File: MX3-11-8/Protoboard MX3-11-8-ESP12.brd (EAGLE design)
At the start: 74.4 x 99.4 mm, 638 parts, among them J1 DCJ0202, X3 RJ45

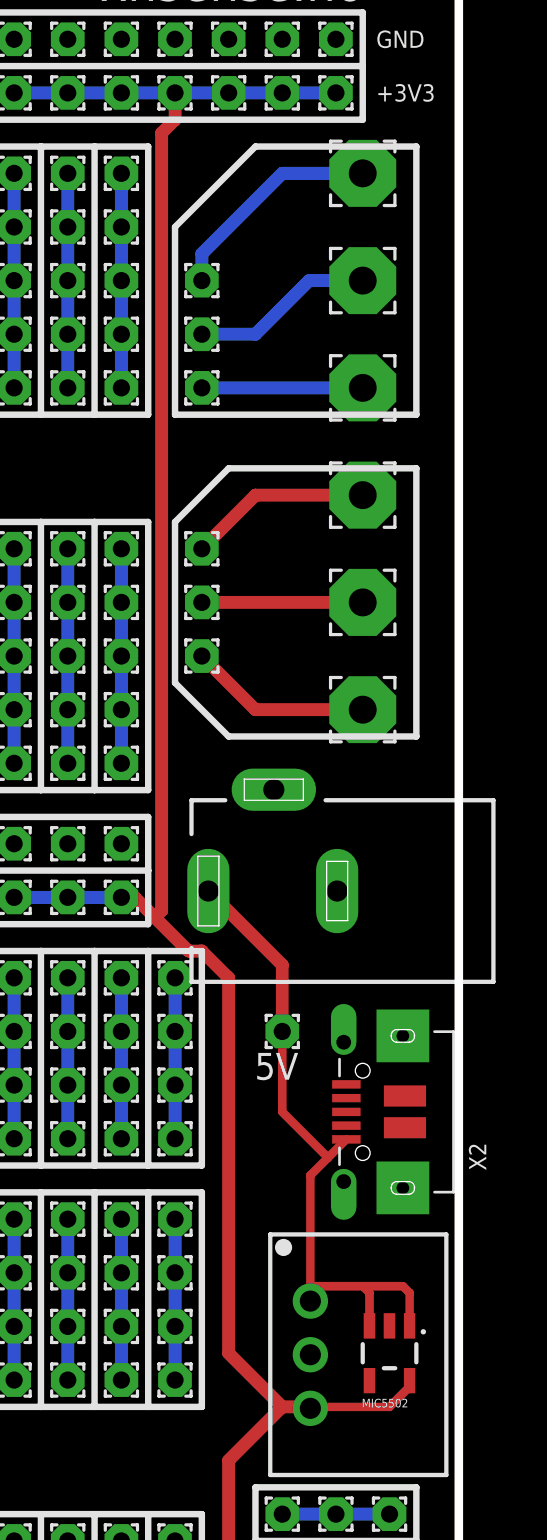
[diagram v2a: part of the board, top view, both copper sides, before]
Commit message: Change usb connector
Change to correct usb connecter and moved esp8266 bit more onto the
board.
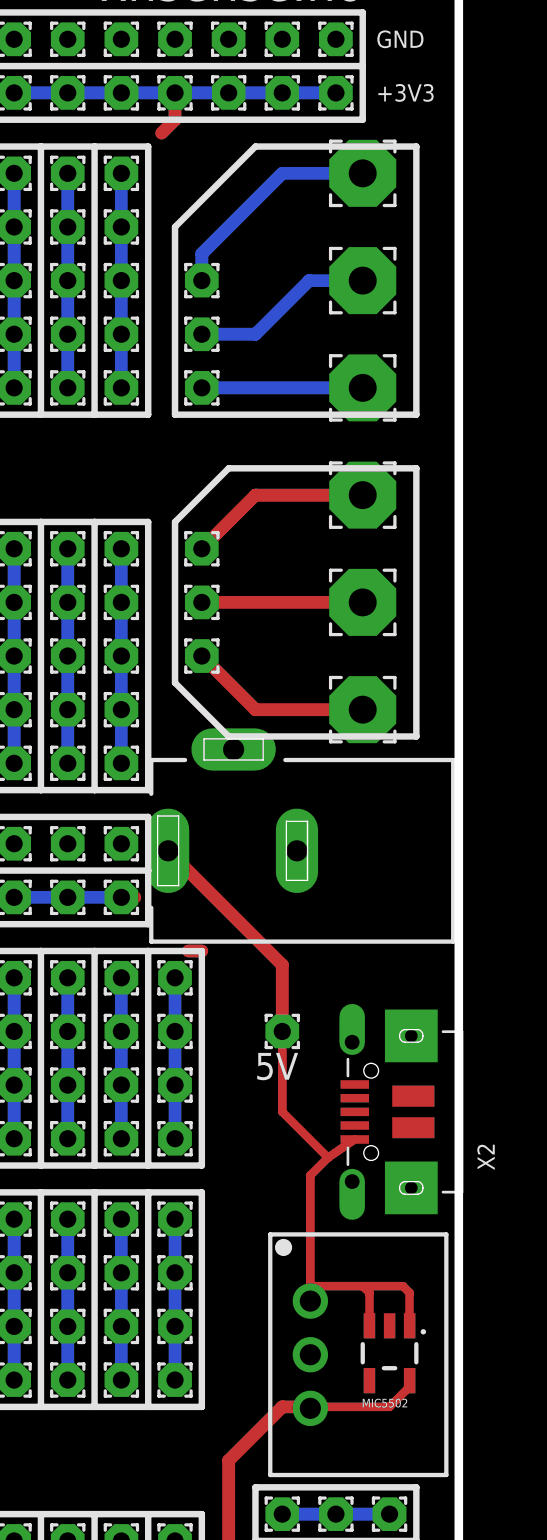
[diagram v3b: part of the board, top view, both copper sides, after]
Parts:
- moved J1 2.69 mm to (63.7, 56.8)
- moved X2 0.40 mm to (70.2, 44.5)
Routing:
- net VDD: track 304.0 -> 239.9 mm
- net VCC: track 31.7 -> 34.7 mm
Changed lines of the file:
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@@
 <attribute name="VALUE" x="17.78" y="6.95" size="0.0254" layer="27"/>
 </element>
-<element name="J1" library="con-jack" package="DCJ0202" value="DCJ0202" x="65.64" y="54.91" smashed="yes" rot="R90">
-<attribute name="MPN" value="" x="65.64" y="54.91" size="1.778" layer="27" rot="R90" display="off"/>
-<attribute name="OC_NEWARK" value="unknown" x="65.64" y="54.91" size="1.778" layer="27" rot="R90" display="off"/>
-<attribute name="MF" value="" x="65.64" y="54.91" size="1.778" layer="27" rot="R90" display="off"/>
-<attribute name="OC_FARNELL" value="unknown" x="65.64" y="54.91" size="1.778" layer="27" rot="R90" display="off"/>
+<element name="J1" library="con-jack" package="DCJ0202" value="DCJ0202" x="63.735" y="56.815" smashed="yes" rot="R90">
+<attribute name="MPN" value="" x="63.735" y="56.815" size="1.778" layer="27" rot="R90" display="off"/>
+<attribute name="OC_NEWARK" value="unknown" x="63.735" y="56.815" size="1.778" layer="27" rot="R90" display="off"/>
+<attribute name="MF" value="" x="63.735" y="56.815" size="1.778" layer="27" rot="R90" display="off"/>
+<attribute name="OC_FARNELL" value="unknown" x="63.735" y="56.815" size="1.778" layer="27" rot="R90" display="off"/>
 </element>
 <element name="DC" library="dc-dc-converter" package="SIP3" value="R-78C1.8-1.0" x="67.37" y="32.95" smashed="yes" rot="R270"/>
@@
 <attribute name="VALUE" x="25.4" y="79.34" size="0.0254" layer="27"/>
 </element>
-<element name="X2" library="microbuilder" package="4UCONN_20329" value="" x="69.85" y="44.45" rot="R90"/>
+<element name="X2" library="microbuilder" package="4UCONN_20329" value="" x="70.25" y="44.45" rot="R90"/>
 <element name="MIC5502" library="SparkFun-PowerIC" package="SOT23-5" value="" x="71.12" y="33.02" rot="R180">
 <attribute name="PROD_ID" value="VREG-00822" x="76.2" y="26.67" size="1.778" layer="27" rot="R180" display="off"/>
@@
 <wire x1="67.37" y1="36.195" x2="67.37" y2="41.445" width="0.4064" layer="1"/>
 <wire x1="67.37" y1="41.445" x2="68.2075" y2="42.2825" width="0.4064" layer="1"/>
-<wire x1="68.2075" y1="42.2825" x2="69.075" y2="43.15" width="0.4064" layer="1"/>
+<wire x1="68.2075" y1="42.2825" x2="69.475" y2="43.15" width="0.4064" layer="1"/>
 <wire x1="72.07" y1="34.3201" x2="72.07" y2="35.88" width="0.4064" layer="1"/>
 <wire x1="72.07" y1="35.88" x2="71.755" y2="36.195" width="0.4064" layer="1"/>
@@
 <wire x1="66.04" y1="44.45" x2="68.2075" y2="42.2825" width="0.4064" layer="1"/>
 <wire x1="66.04" y1="48.26" x2="66.04" y2="51.41" width="0.6096" layer="1"/>
-<wire x1="66.04" y1="51.41" x2="62.54" y2="54.91" width="0.6096" layer="1"/>
+<wire x1="66.04" y1="51.41" x2="60.635" y2="56.815" width="0.6096" layer="1"/>
 </signal>
 <signal name="VDD">
@@
 <wire x1="71.12" y1="30.48" x2="67.44" y2="30.48" width="0.4064" layer="1"/>
 <wire x1="67.44" y1="30.48" x2="67.37" y2="30.41" width="0.4064" layer="1"/>
-<wire x1="66.04" y1="30.48" x2="63.5" y2="33.02" width="0.6096" layer="1"/>
-<wire x1="63.5" y1="33.02" x2="63.5" y2="50.8" width="0.6096" layer="1"/>
-<wire x1="63.5" y1="50.8" x2="62.23" y2="52.07" width="0.6096" layer="1"/>
 <wire x1="62.23" y1="52.07" x2="61.595" y2="52.07" width="0.6096" layer="1"/>
-<wire x1="61.595" y1="52.07" x2="60.0075" y2="53.6575" width="0.6096" layer="1"/>
-<wire x1="60.0075" y1="53.6575" x2="59.055" y2="54.61" width="0.6096" layer="1"/>
 <wire x1="59.055" y1="54.61" x2="58.42" y2="54.61" width="0.6096" layer="1"/>
 <wire x1="60.96" y1="92.71" x2="60.96" y2="91.44" width="0.6096" layer="1"/>
 <wire x1="60.96" y1="91.44" x2="60.325" y2="90.805" width="0.6096" layer="1"/>
-<wire x1="60.325" y1="90.805" x2="60.325" y2="53.975" width="0.6096" layer="1"/>
-<wire x1="60.325" y1="53.975" x2="60.0075" y2="53.6575" width="0.6096" layer="1"/>
 <wire x1="58.42" y1="54.61" x2="10.16" y2="54.61" width="0.6096" layer="16"/>
 <wire x1="2.54" y1="92.71" x2="68.58" y2="92.71" width="0.6096" layer="16"/>
 <wire x1="63.5" y1="92.71" x2="66.04" y2="92.71" width="0" layer="19" extent="1-1"/>
+<wire x1="60.96" y1="92.71" x2="63.5" y2="92.71" width="0" layer="19" extent="1-1"/>
+<wire x1="58.42" y1="92.71" x2="60.96" y2="92.71" width="0" layer="19" extent="1-1"/>
+<wire x1="55.88" y1="92.71" x2="58.42" y2="92.71" width="0" layer="19" extent="1-1"/>
+<wire x1="53.34" y1="92.71" x2="55.88" y2="92.71" width="0" layer="19" extent="1-1"/>
+<wire x1="50.8" y1="92.71" x2="53.34" y2="92.71" width="0" layer="19" extent="1-1"/>
+<wire x1="48.26" y1="92.71" x2="50.8" y2="92.71" width="0" layer="19" extent="1-1"/>
+<wire x1="45.72" y1="92.71" x2="48.26" y2="92.71" width="0" layer="19" extent="1-1"/>
+<wire x1="43.18" y1="92.71" x2="45.72" y2="92.71" width="0" layer="19" extent="1-1"/>
+<wire x1="40.64" y1="92.71" x2="43.18" y2="92.71" width="0" layer="19" extent="1-1"/>
+<wire x1="38.1" y1="92.71" x2="40.64" y2="92.71" width="0" layer="19" extent="1-1"/>
+<wire x1="35.56" y1="92.71" x2="38.1" y2="92.71" width="0" layer="19" extent="1-1"/>
+<wire x1="33.02" y1="92.71" x2="35.56" y2="92.71" width="0" layer="19" extent="1-1"/>
+<wire x1="30.48" y1="92.71" x2="33.02" y2="92.71" width="0" layer="19" extent="1-1"/>
+<wire x1="27.94" y1="92.71" x2="30.48" y2="92.71" width="0" layer="19" extent="1-1"/>
+<wire x1="25.4" y1="92.71" x2="27.94" y2="92.71" width="0" layer="19" extent="1-1"/>
+<wire x1="22.86" y1="92.71" x2="25.4" y2="92.71" width="0" layer="19" extent="1-1"/>
+<wire x1="20.32" y1="92.71" x2="22.86" y2="92.71" width="0" layer="19" extent="1-1"/>
+<wire x1="17.78" y1="92.71" x2="20.32" y2="92.71" width="0" layer="19" extent="1-1"/>
+<wire x1="15.24" y1="92.71" x2="17.78" y2="92.71" width="0" layer="19" extent="1-1"/>
+<wire x1="12.7" y1="92.71" x2="15.24" y2="92.71" width="0" layer="19" extent="1-1"/>
+<wire x1="10.16" y1="92.71" x2="12.7" y2="92.71" width="0" layer="19" extent="1-1"/>
+<wire x1="7.62" y1="92.71" x2="10.16" y2="92.71" width="0" layer="19" extent="1-1"/>
+<wire x1="5.08" y1="92.71" x2="7.62" y2="92.71" width="0" layer="19" extent="1-1"/>
 <wire x1="68.58" y1="92.71" x2="66.04" y2="92.71" width="0" layer="19" extent="1-1"/>
-<wire x1="5.08" y1="92.71" x2="2.54" y2="92.71" width="0" layer="19" extent="1-1"/>
-<wire x1="7.62" y1="92.71" x2="5.08" y2="92.71" width="0" layer="19" extent="1-1"/>
-<wire x1="10.16" y1="92.71" x2="7.62" y2="92.71" width="0" layer="19" extent="1-1"/>
-<wire x1="12.7" y1="92.71" x2="10.16" y2="92.71" width="0" layer="19" extent="1-1"/>
-<wire x1="15.24" y1="92.71" x2="12.7" y2="92.71" width="0" layer="19" extent="1-1"/>
-<wire x1="17.78" y1="92.71" x2="15.24" y2="92.71" width="0" layer="19" extent="1-1"/>
-<wire x1="20.32" y1="92.71" x2="17.78" y2="92.71" width="0" layer="19" extent="1-1"/>
-<wire x1="22.86" y1="92.71" x2="20.32" y2="92.71" width="0" layer="19" extent="1-1"/>
-<wire x1="25.4" y1="92.71" x2="22.86" y2="92.71" width="0" layer="19" extent="1-1"/>
-<wire x1="27.94" y1="92.71" x2="25.4" y2="92.71" width="0" layer="19" extent="1-1"/>
-<wire x1="30.48" y1="92.71" x2="27.94" y2="92.71" width="0" layer="19" extent="1-1"/>
-<wire x1="33.02" y1="92.71" x2="30.48" y2="92.71" width="0" layer="19" extent="1-1"/>
-<wire x1="35.56" y1="92.71" x2="33.02" y2="92.71" width="0" layer="19" extent="1-1"/>
-<wire x1="38.1" y1="92.71" x2="35.56" y2="92.71" width="0" layer="19" extent="1-1"/>
-<wire x1="40.64" y1="92.71" x2="38.1" y2="92.71" width="0" layer="19" extent="1-1"/>
-<wire x1="43.18" y1="92.71" x2="40.64" y2="92.71" width="0" layer="19" extent="1-1"/>
-<wire x1="45.72" y1="92.71" x2="43.18" y2="92.71" width="0" layer="19" extent="1-1"/>
-<wire x1="48.26" y1="92.71" x2="45.72" y2="92.71" width="0" layer="19" extent="1-1"/>
-<wire x1="50.8" y1="92.71" x2="48.26" y2="92.71" width="0" layer="19" extent="1-1"/>
-<wire x1="53.34" y1="92.71" x2="50.8" y2="92.71" width="0" layer="19" extent="1-1"/>
-<wire x1="55.88" y1="92.71" x2="53.34" y2="92.71" width="0" layer="19" extent="1-1"/>
-<wire x1="58.42" y1="92.71" x2="55.88" y2="92.71" width="0" layer="19" extent="1-1"/>
-<wire x1="60.96" y1="92.71" x2="63.5" y2="92.71" width="0" layer="19" extent="1-1"/>
+<wire x1="59.055" y1="54.61" x2="60.325" y2="90.805" width="0" layer="19" extent="1-1"/>
 <wire x1="55.88" y1="54.61" x2="58.42" y2="54.61" width="0" layer="19" extent="1-1"/>
 <wire x1="53.34" y1="54.61" x2="55.88" y2="54.61" width="0" layer="19" extent="1-1"/>
@@
 <wire x1="20.32" y1="54.61" x2="22.86" y2="54.61" width="0" layer="19" extent="1-1"/>
 <wire x1="17.78" y1="54.61" x2="20.32" y2="54.61" width="0" layer="19" extent="1-1"/>
+<wire x1="15.24" y1="54.61" x2="17.78" y2="54.61" width="0" layer="19" extent="1-1"/>
+<wire x1="12.7" y1="54.61" x2="10.16" y2="54.61" width="0" layer="19" extent="1-1"/>
+<wire x1="61.595" y1="52.07" x2="59.055" y2="54.61" width="0" layer="19" extent="1-1"/>
+<wire x1="66.04" y1="30.48" x2="62.23" y2="52.07" width="0" layer="19" extent="1-1"/>
 <wire x1="66.04" y1="6.35" x2="63.5" y2="6.35" width="0" layer="19" extent="1-1"/>
-<wire x1="15.24" y1="54.61" x2="17.78" y2="54.61" width="0" layer="19" extent="1-1"/>
 <wire x1="60.96" y1="6.35" x2="63.5" y2="6.35" width="0" layer="19" extent="1-1"/>
-<wire x1="12.7" y1="54.61" x2="10.16" y2="54.61" width="0" layer="19" extent="1-1"/>
 <wire x1="58.42" y1="6.35" x2="60.96" y2="6.35" width="0" layer="19" extent="1-1"/>
 <wire x1="55.88" y1="6.35" x2="58.42" y2="6.35" width="0" layer="19" extent="1-1"/>

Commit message: Update esp component and usb
test
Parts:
- removed MDL2: (no value), ESP8266-ESP12E:ESP8266-ESP12E
- added X1: ESP-12E, microbuilder:ESP-12E
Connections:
- removed net N$58: MDL2.21, PAD762.1, PAD763.1, PAD764.1, PAD765.1
- removed net N$85: MDL2.20, PAD766.1, PAD767.1, PAD768.1, PAD769.1
- new net N$29: PAD762.1, PAD763.1, PAD764.1, PAD765.1
- new net N$30: PAD766.1, PAD767.1, PAD768.1, PAD769.1
- net GND: now also X1.9; no longer MDL2.9
- net N$113: now also X1.3; no longer MDL2.3
- net N$121: now also X1.7; no longer MDL2.7
- net N$122: no longer MDL2.18
- net N$47: now also X1.14; no longer MDL2.14
- net N$48: now also X1.13; no longer MDL2.13
- net N$52: now also X1.12; no longer MDL2.12
- net N$53: now also X1.11; no longer MDL2.11
- net N$54: now also X1.10; no longer MDL2.10
- net N$55: no longer MDL2.22
- net N$56: now also X1.5; no longer MDL2.5
- net N$57: no longer MDL2.17
- net N$86: no longer MDL2.19
- net N$87: now also X1.1; no longer MDL2.1
- net N$88: now also X1.2; no longer MDL2.2
- net N$90: now also X1.4; no longer MDL2.4
- net N$91: now also X1.6; no longer MDL2.6
- net RX: now also X1.15; no longer MDL2.15
- net TX: now also X1.16; no longer MDL2.16
- net VDD: now also X1.8; no longer MDL2.8
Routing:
- net VDD: track 239.9 -> 322.9 mm, vias 1 -> 0
- net N$85: track 22.2 -> 0.00 mm
- net N$58: track 20.2 -> 0.00 mm
- net N$86: track 21.5 -> 8.34 mm
- net N$122: track 19.6 -> 8.68 mm
- net N$55: track 17.9 -> 8.19 mm
- net N$57: track 17.4 -> 8.68 mm
- net N$30: track 0.00 -> 8.49 mm
- net N$29: track 0.00 -> 8.19 mm
- net N$73: track 10.2 -> 12.0 mm
- net N$77: track 10.2 -> 12.0 mm
- net N$110: track 10.2 -> 12.0 mm
- net N$81: track 10.2 -> 11.9 mm
- net N$98: track 10.2 -> 11.9 mm
- net TX: track 56.1 -> 54.5 mm
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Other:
- board text removed: "10"
- board text removed: "9"
- board text removed: "CSO"
- board text removed: "MISO"
- board text removed: "MOSI"
- board text removed: "SCLK"
